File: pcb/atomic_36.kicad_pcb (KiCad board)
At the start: 2 copper layers, 133.8 x 99 mm, 47 parts, among them J1 USB_C_12P

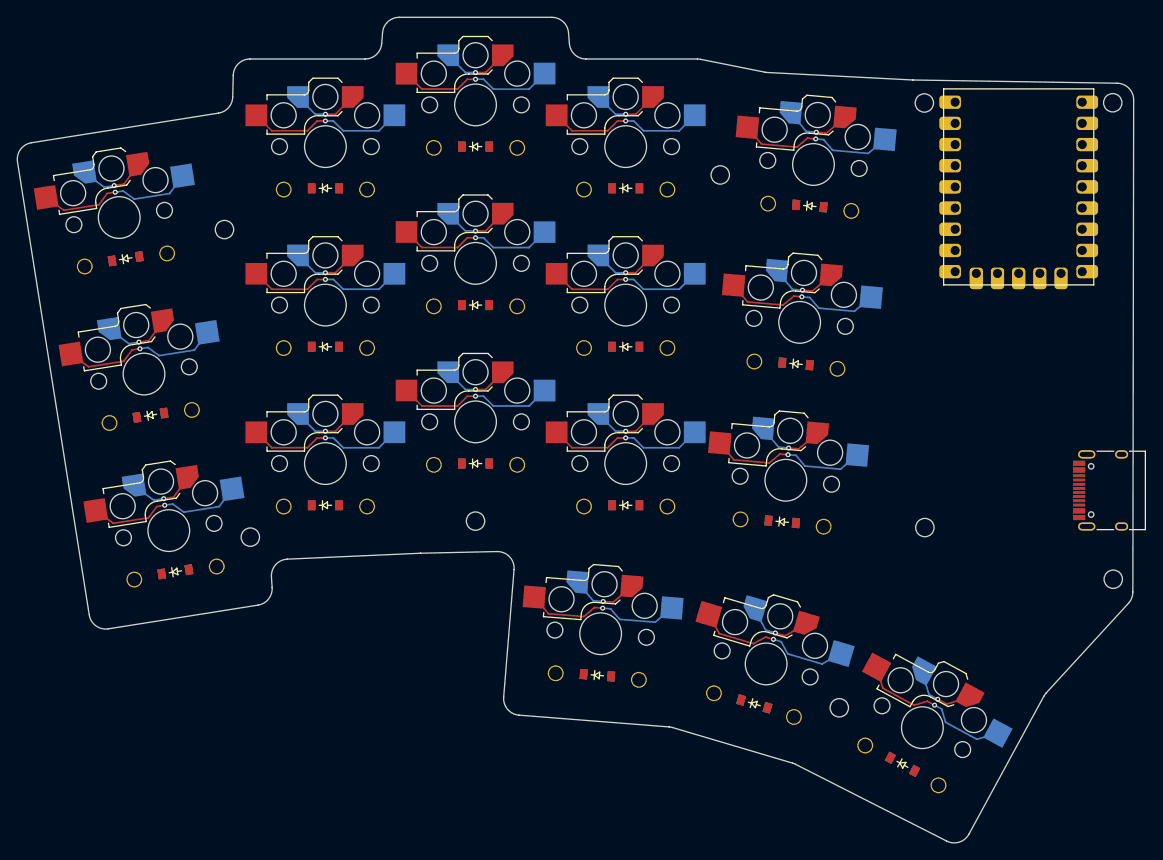
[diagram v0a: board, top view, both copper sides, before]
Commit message: Begin routing the left side (diodes and switches on back)
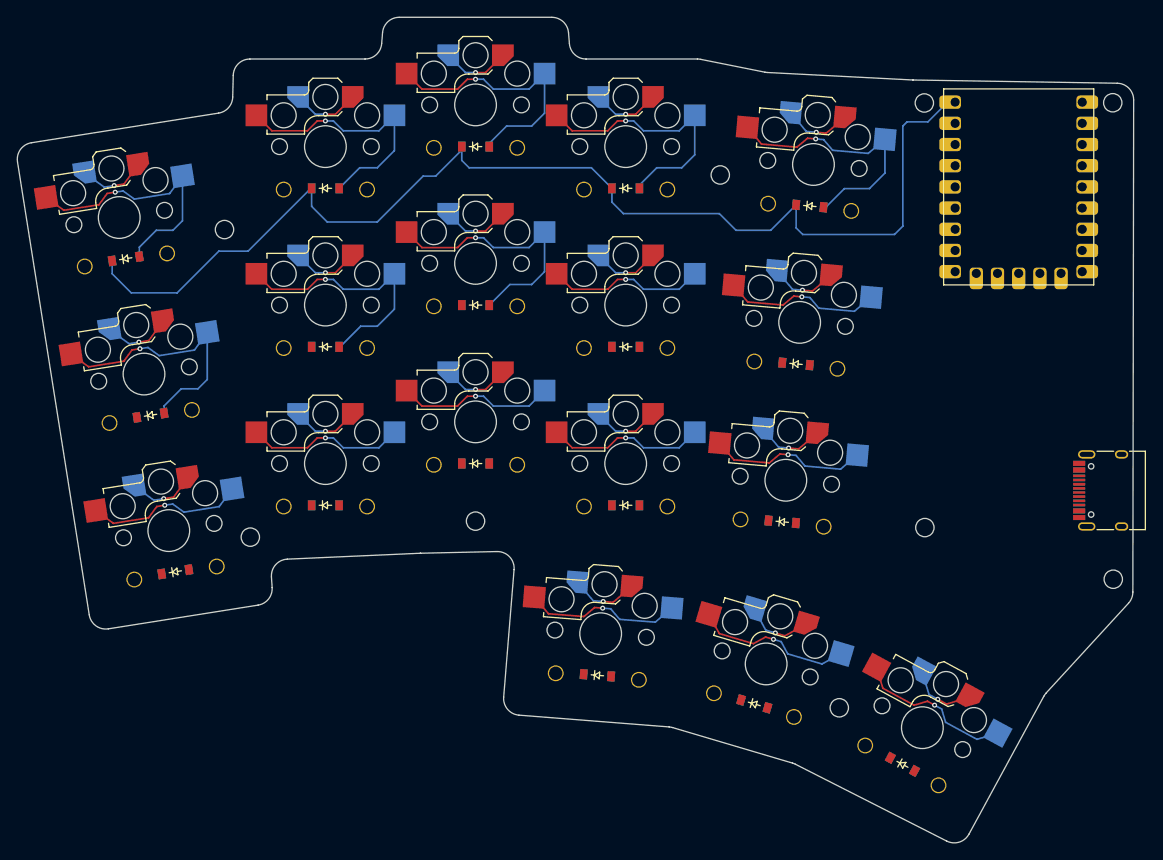
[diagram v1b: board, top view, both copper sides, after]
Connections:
- J1 pad F11: VBUS -> P5V
- J1 pad F2: VBUS -> P5V
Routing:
- net GP0: track 0.00 -> 139.7 mm
- net middle_top: track 19.1 -> 32.3 mm
- net index_top: track 19.1 -> 32.3 mm
- net ring_home: track 19.1 -> 32.2 mm
- net inner_top: track 19.1 -> 32.2 mm
- net middle_home: track 19.1 -> 32.1 mm
- net pinky_top: track 19.1 -> 32.1 mm
- net pinky_home: track 19.1 -> 32.1 mm
- net ring_top: track 19.1 -> 31.8 mm

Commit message: Add PCB with MCU up config
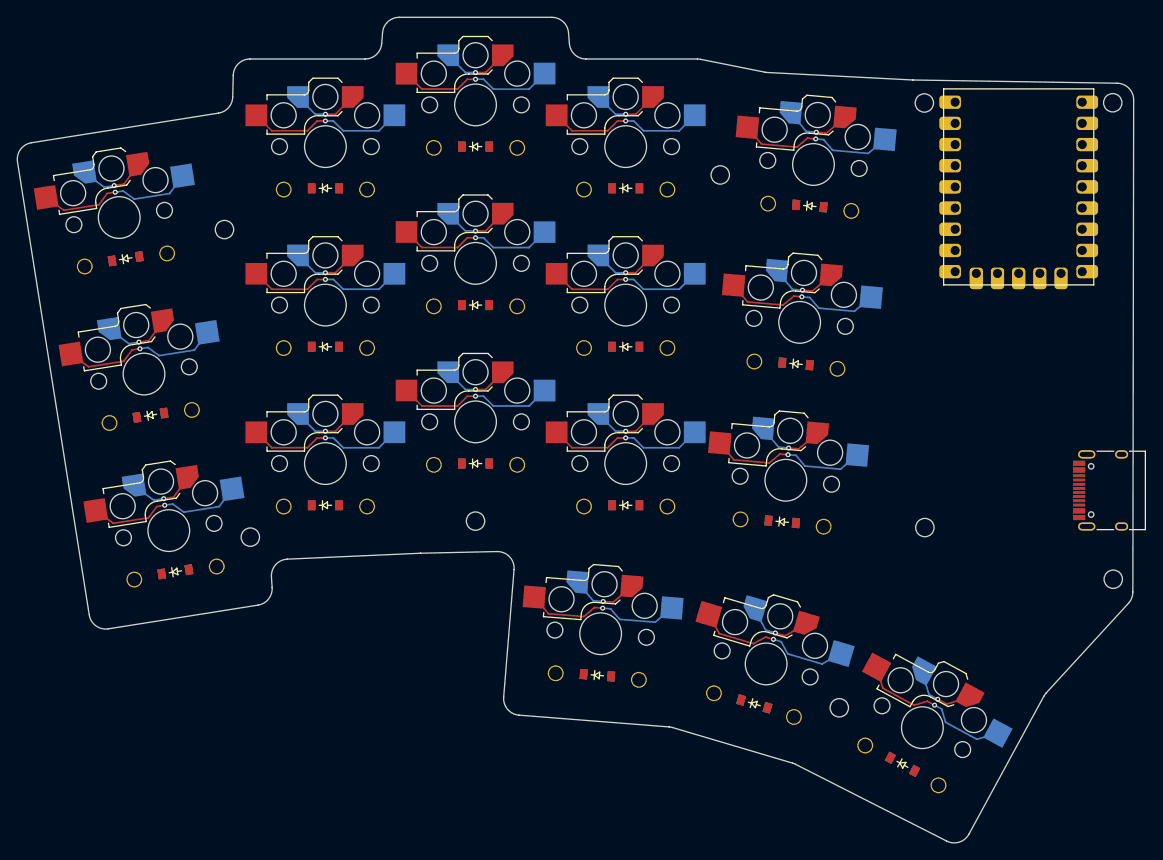
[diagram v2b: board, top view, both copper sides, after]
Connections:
- D1 pad 1: GP2 -> GP27
- D10 pad 1: GP2 -> GP27
- D11 pad 1: GP1 -> GP28
- D12 pad 1: GP0 -> GP29
- D13 pad 1: GP2 -> GP27
- D14 pad 1: GP1 -> GP28
- D15 pad 1: GP0 -> GP29
- D16 pad 1: GP3 -> GP26
- D17 pad 1: GP3 -> GP26
- D18 pad 1: GP3 -> GP26
- D2 pad 1: GP1 -> GP28
- D3 pad 1: GP0 -> GP29
- D4 pad 1: GP2 -> GP27
- D5 pad 1: GP1 -> GP28
- D6 pad 1: GP0 -> GP29
- D7 pad 1: GP2 -> GP27
- D8 pad 1: GP1 -> GP28
- D9 pad 1: GP0 -> GP29
- J1 pad F11: P5V -> VBUS
- J1 pad F2: P5V -> VBUS
- S1 pad 1: GP4 -> GP15
- S10 pad 1: GP7 -> GP12
- S11 pad 1: GP7 -> GP12
- S12 pad 1: GP7 -> GP12
- S13 pad 1: GP8 -> GP11
- S14 pad 1: GP8 -> GP11
- S15 pad 1: GP8 -> GP11
- S16 pad 1: GP6 -> GP13
- S17 pad 1: GP7 -> GP12
- S18 pad 1: GP8 -> GP11
- S2 pad 1: GP4 -> GP15
- S3 pad 1: GP4 -> GP15
- S4 pad 1: GP5 -> GP14
- S5 pad 1: GP5 -> GP14
- S6 pad 1: GP5 -> GP14
- S7 pad 1: GP6 -> GP13
- S8 pad 1: GP6 -> GP13
- S9 pad 1: GP6 -> GP13
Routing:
- net GP0: track 139.7 -> 0.00 mm
- net GP6: track 33.1 -> 0.00 mm, vias 4 -> 0
- net GP11: track 0.00 -> 33.1 mm, vias 0 -> 4
- net GP7: track 33.1 -> 0.00 mm, vias 4 -> 0
- net GP13: track 0.00 -> 33.1 mm, vias 0 -> 4
- net GP12: track 0.00 -> 33.1 mm, vias 0 -> 4
- net GP8: track 33.1 -> 0.00 mm, vias 4 -> 0
- net GP14: track 0.00 -> 24.8 mm, vias 0 -> 3
- net GP5: track 24.8 -> 0.00 mm, vias 3 -> 0
- net GP15: track 0.00 -> 24.8 mm, vias 0 -> 3
- net GP4: track 24.8 -> 0.00 mm, vias 3 -> 0
- net middle_top: track 32.3 -> 19.1 mm
- net index_top: track 32.3 -> 19.1 mm
- net ring_home: track 32.2 -> 19.1 mm
- net inner_top: track 32.2 -> 19.1 mm
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
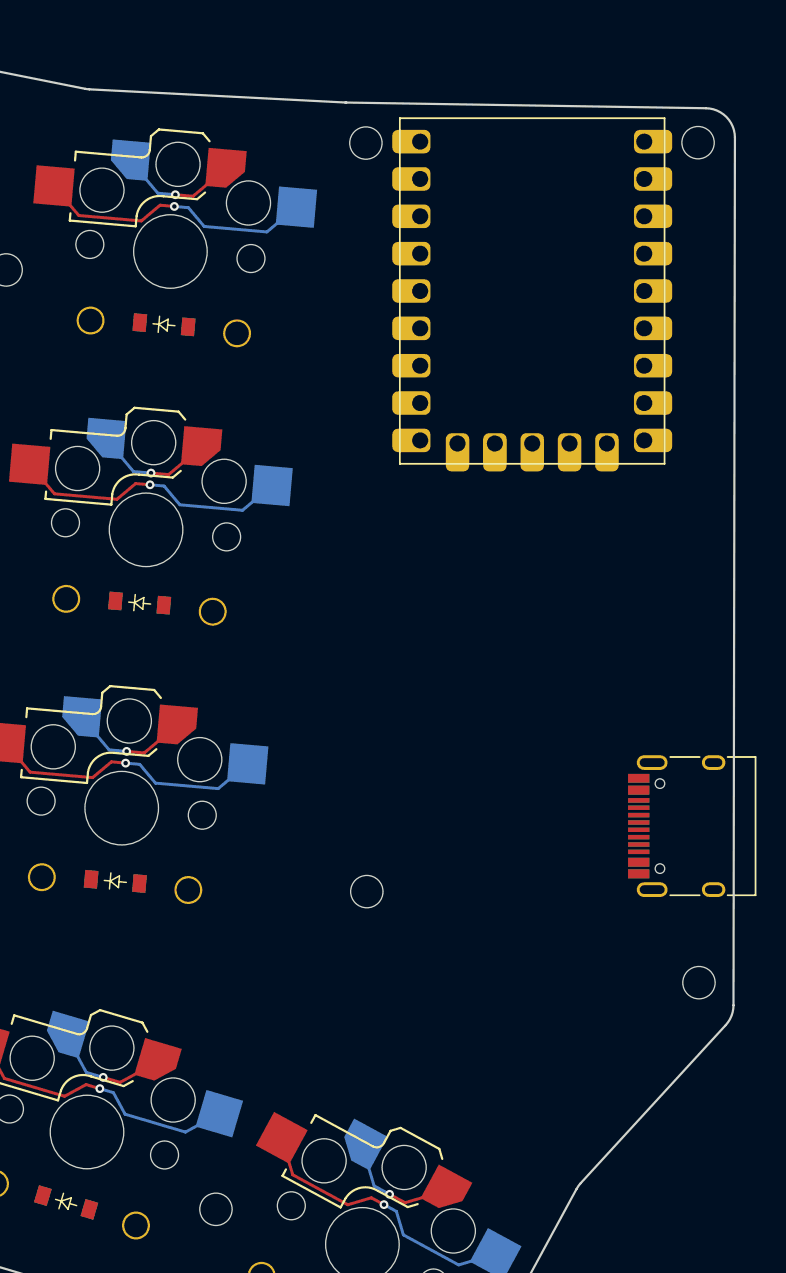
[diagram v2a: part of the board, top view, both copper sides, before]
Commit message: Adjust top right side, make flat
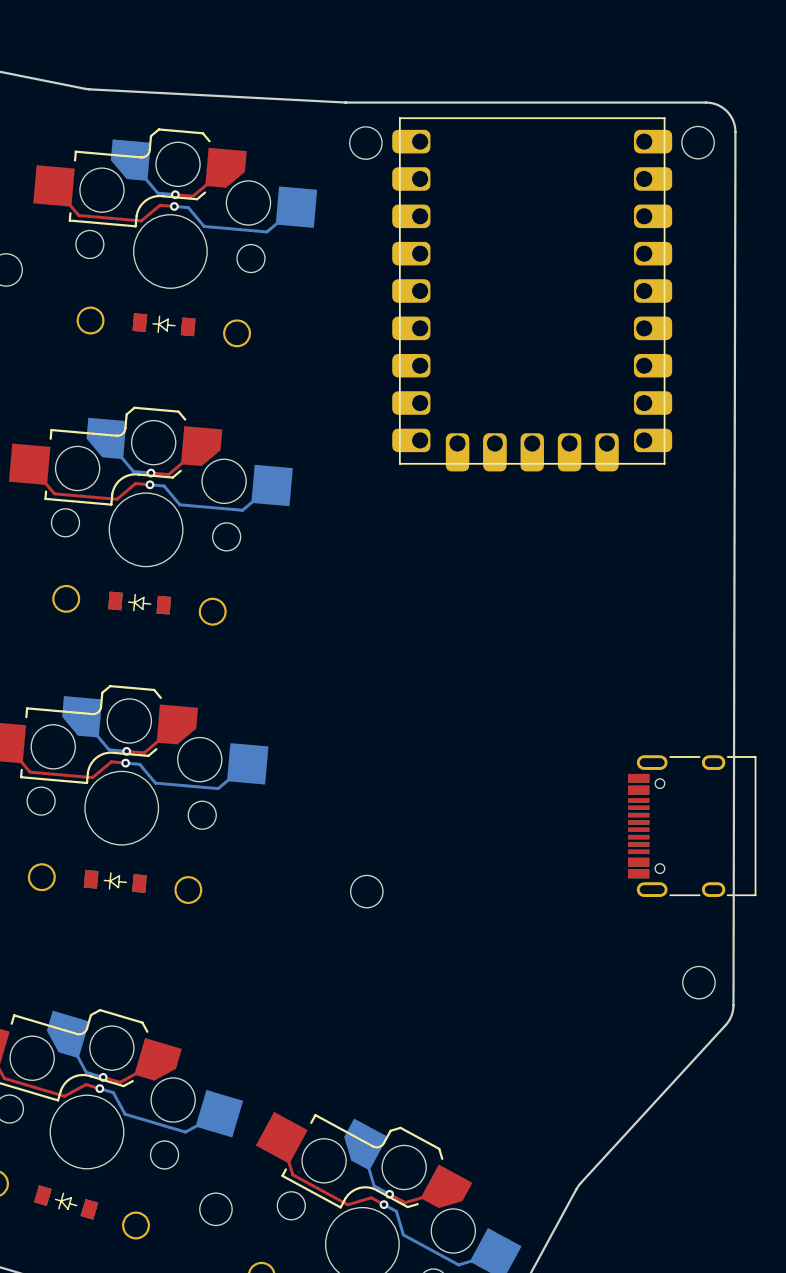
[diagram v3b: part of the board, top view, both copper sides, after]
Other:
- board size 133.8 x 99 mm -> 133.9 x 99 mm
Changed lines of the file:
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@@
 (gr_line (start 200.02044662905516 93.46415580000001) (end 213.37615078728166 93.46415580000001) (layer Edge.Cuts) (stroke (width 0.15) (type default)))
 (gr_line (start 213.76812440650025 93.5029427038411) (end 221.48302188171854 95.04486405749444) (layer Edge.Cuts) (stroke (width 0.15) (type default)))
-(gr_line (start 221.77206850581172 95.08100066673991) (end 239.1785148078376 95.97798663299808) (layer Edge.Cuts) (stroke (width 0.15) (type default)))
-(gr_line (start 239.24984820293795 95.9803873291732) (end 263.7067661319504 96.36677726529493) (layer Edge.Cuts) (stroke (width 0.15) (type default)))
-(gr_line (start 265.67516983192525 98.36982866699691) (end 265.5777931038819 157.3673418412509) (layer Edge.Cuts) (stroke (width 0.15) (type default)))
-(gr_line (start 265.05140065817125 158.71625709090364) (end 255.185678340181 169.46762672427838) (layer Edge.Cuts) (stroke (width 0.15) (type default)))
+(gr_line (start 221.77206850581172 95.08100066673991) (end 239.1627186048911 95.97717262581263) (layer Edge.Cuts) (stroke (width 0.15) (type default)))
+(gr_line (start 239.2656682000165 95.97982292040713) (end 263.7105457971998 95.97954785537891) (layer Edge.Cuts) (stroke (width 0.15) (type default)))
+(gr_line (start 265.7105633969769 97.98400445540028) (end 265.5782403300698 157.36800756063894) (layer Edge.Cuts) (stroke (width 0.15) (type default)))
+(gr_line (start 265.0518501845748 158.71576721045) (end 255.18567834018106 169.46762672427826) (layer Edge.Cuts) (stroke (width 0.15) (type default)))
 (gr_line (start 254.90164903640235 169.8655253968621) (end 245.92723320329497 186.39434324637898) (layer Edge.Cuts) (stroke (width 0.15) (type default)))
 (gr_line (start 243.26402102472665 187.22326110951855) (end 225.12312321319678 178.01079259897443) (layer Edge.Cuts) (stroke (width 0.15) (type default)))
@@
 (gr_arc (start 213.76812438728166 93.50294270000002) (mid 213.57309478728166 93.47387610000001) (end 213.37615078728166 93.46415580000001) (layer Edge.Cuts) (stroke (width 0.15) (type default)))
 (gr_arc (start 221.4830219009371 95.04486406133552) (mid 221.6268864009371 95.06820176133552) (end 221.7720685009371 95.08100076133552) (layer Edge.Cuts) (stroke (width 0.15) (type default)))
-(gr_arc (start 239.17851480296292 95.9779867275937) (mid 239.2141708029629 95.97950532759371) (end 239.2498482029629 95.98038742759371) (layer Edge.Cuts) (stroke (width 0.15) (type default)))
-(gr_arc (start 265.6751698319255 98.3698286668744) (mid 265.1016697319254 96.9647052668744) (end 263.70676613192546 96.3667771668744) (layer Edge.Cuts) (stroke (width 0.15) (type default)))
-(gr_arc (start 265.05140060388214 158.71625704108652) (mid 265.44095730388216 158.09110954108652) (end 265.57779300388216 157.36734184108653) (layer Edge.Cuts) (stroke (width 0.15) (type default)))
+(gr_arc (start 239.16271860001643 95.97717272040825) (mid 239.21417630001642 95.97916062040825) (end 239.26566820001642 95.97982292040825) (layer Edge.Cuts) (stroke (width 0.15) (type default)))
+(gr_arc (start 265.7105633971998 97.98400445537779) (mid 265.1263486971998 96.56690285537779) (end 263.71054579719976 95.97954785537779) (layer Edge.Cuts) (stroke (width 0.15) (type default)))
+(gr_arc (start 265.05185013029256 158.71576716063925) (mid 265.4411967302926 158.09115796063926) (end 265.5782403302926 157.36800756063926) (layer Edge.Cuts) (stroke (width 0.15) (type default)))
 (gr_arc (start 255.1856783944688 169.46762677409413) (mid 255.0314603944688 169.6578650740941) (end 254.9016490944688 169.86552537409412) (layer Edge.Cuts) (stroke (width 0.15) (type default)))
 (gr_arc (start 243.26402104522847 187.22326106914701) (mid 244.76396944522847 187.34966536914703) (end 245.92723324522848 186.39434326914702) (layer Edge.Cuts) (stroke (width 0.15) (type default)))
